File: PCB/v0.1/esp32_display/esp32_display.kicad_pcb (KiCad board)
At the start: 2 copper layers, 90.5 x 69 mm, 52 parts, among them J1 USB_B_Micro, J2 Conn_01x06_Male, SW1 RST_BTN, SW2 SCREEN_OFF_BTN, U1 ESP32-WROOM-32, U2 MAX1821, U3 Display_ILI9341

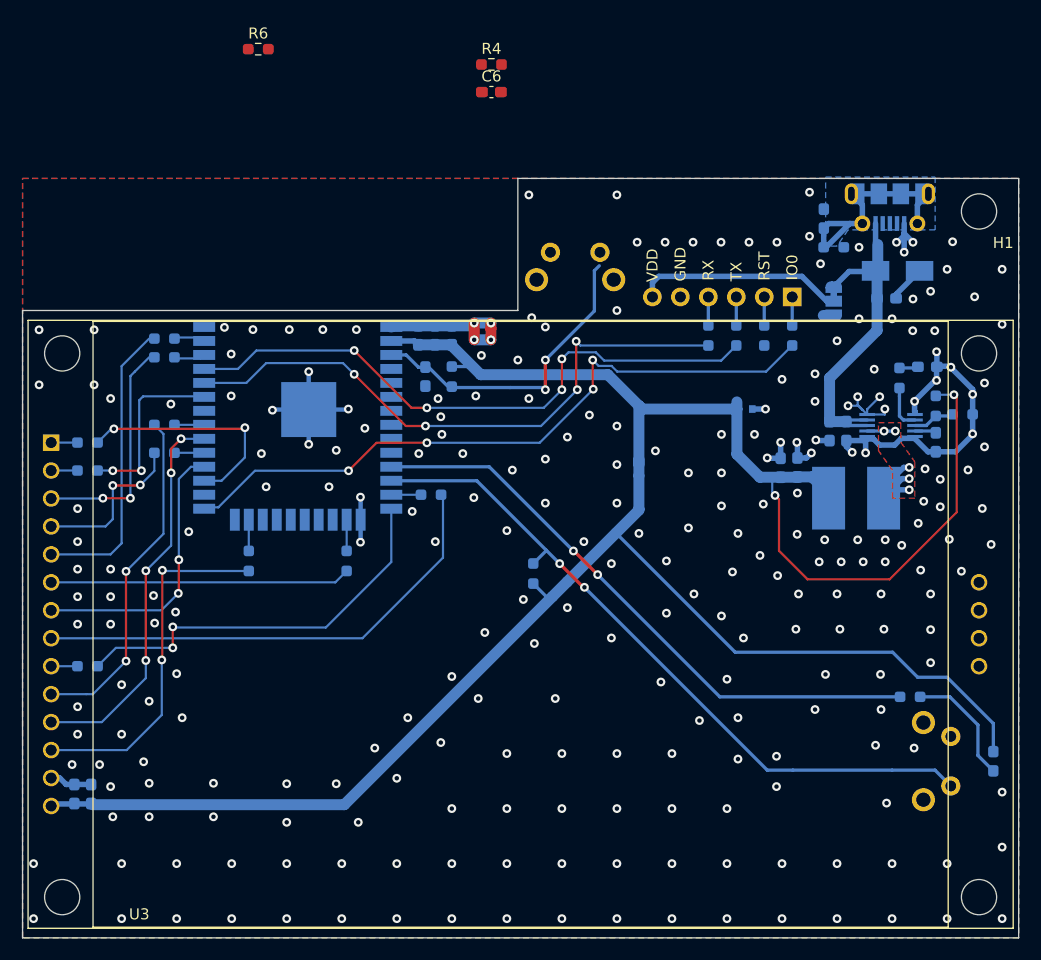
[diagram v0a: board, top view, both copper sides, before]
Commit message: Place RC filters (close to buttons)
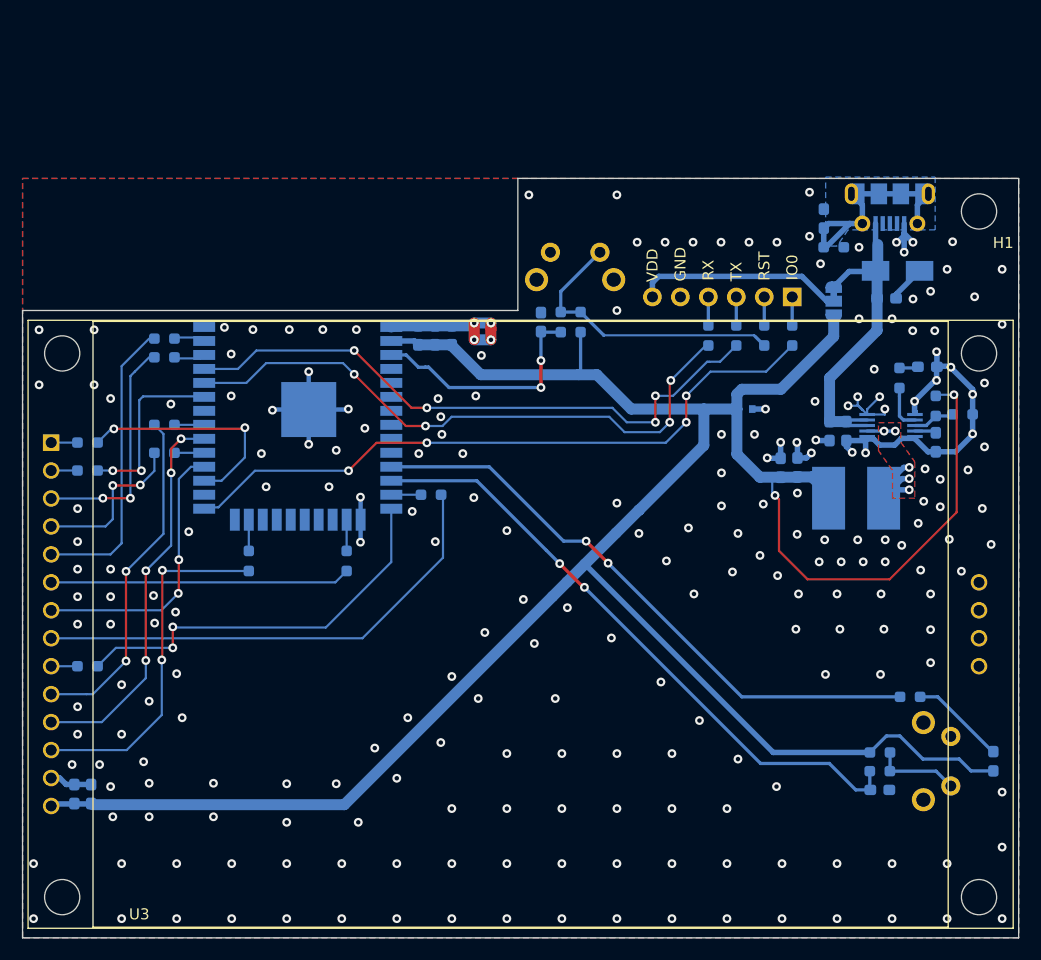
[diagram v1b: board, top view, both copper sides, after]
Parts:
- C6, R4, R6: moved to B.Cu
- moved R4 73.3 mm to (164.9, 85.9)
- moved C6 72.6 mm to (164.9, 87.6)
- moved R6 37.0 mm to (135.9, 45.1), turned to -90 degrees
- moved R3 35.4 mm to (164.9, 84.2), turned to 0 degrees
- moved R5 12.7 mm to (137.7, 45.1), turned to 90 degrees
- moved C7 11.6 mm to (134.1, 45.1), turned to 90 degrees
- turned D3 to -90 degrees
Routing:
- net /MCU/SCRN_OFF_BTN: track 0.00 -> 56.9 mm, vias 0 -> 2
- net Net-(R3-Pad2): track 64.0 -> 7.80 mm, vias 2 -> 0
- net /MCU/RST: track 0.00 -> 26.7 mm
- net +3V3: track 212.1 -> 228.3 mm
- net Net-(C7-Pad1): track 28.6 -> 21.7 mm
- net Net-(D3-Pad1): track 11.1 -> 8.71 mm
- net /MCU/IO0: track 62.1 -> 61.0 mm
- net GND: vias 258 -> 229

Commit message: Dont route L of buck converter through vias
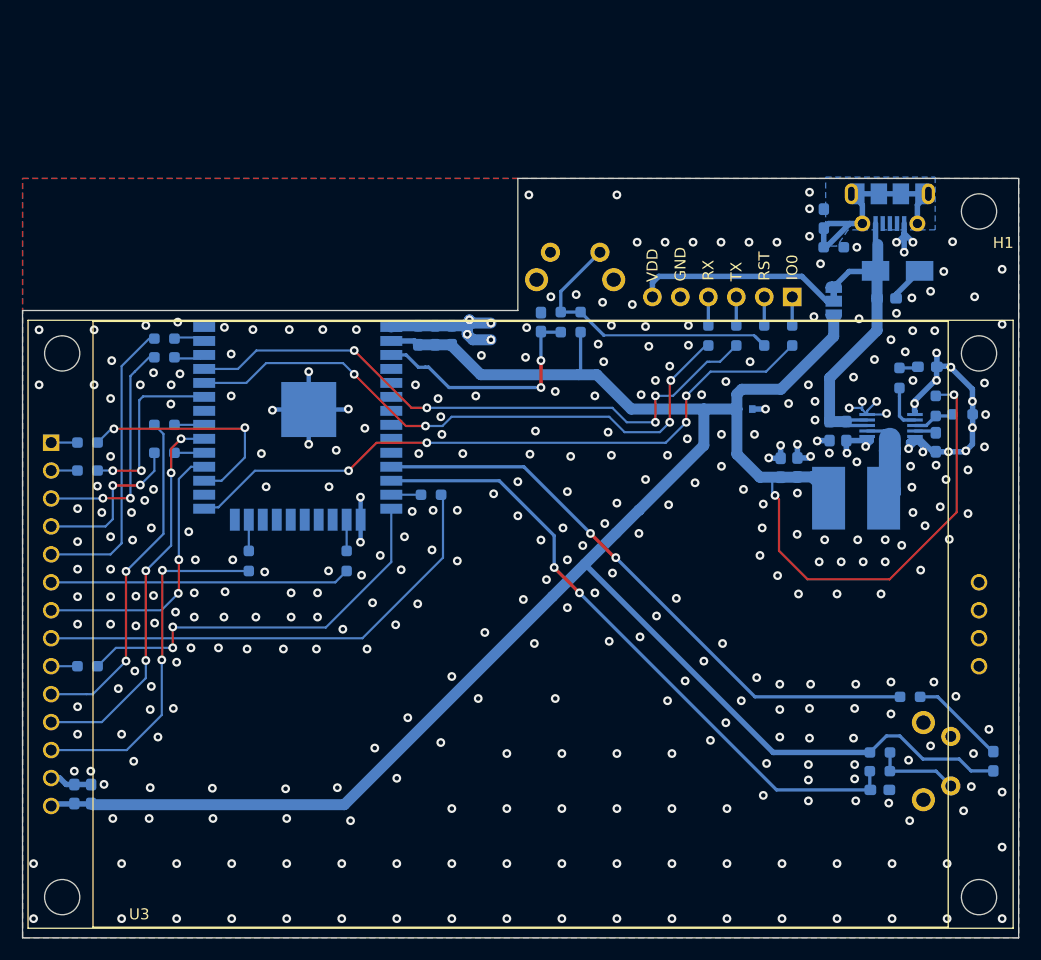
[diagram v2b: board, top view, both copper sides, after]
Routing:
- net GND: track 89.9 -> 84.6 mm, vias 229 -> 361
- net Net-(L1-Pad1): track 11.4 -> 8.19 mm, vias 5 -> 0
- net /MCU/SCRN_OFF_BTN: track 56.9 -> 58.6 mm
- removed copper zone on F.Cu, net Net-(L1-Pad1)

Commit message: Fix 3d models, generate outputs, add .wrl to outputs
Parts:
- J1: footprint Connector_USB:USB_Micro-B_Molex-105017-0001 -> myLib:USB_Micro-B_Molex-105017-0001

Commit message: Buck converter feedback line on top
PCB name and version generated with KiBuzzard
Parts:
- removed the G*** at (148.9, 90.8)
- added G***: LOGO, myLib:tabaluga_5x5, B.Cu at (103.2, 92.8)
- added kibuzzard-61D6E91A: G***, kibuzzard-61D6E91A, B.Cu at (137.2, 81.7)
- moved R19 2.81 mm to (172.6, 53.6), turned to 180 degrees
- moved R20 2.09 mm to (170.8, 52.1), turned to 180 degrees
- moved L1 0.47 mm to (162.7, 60.6)
- moved C10 0.33 mm to (170.0, 56.3)
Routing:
- net GND: track 84.6 -> 74.4 mm, vias 361 -> 367
- net +3V3: track 228.3 -> 224.8 mm, vias 2 -> 0
- net Net-(R19-Pad2): track 3.84 -> 5.48 mm
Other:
- board text added: "BCKL_OFF"
- board text removed: "DISP_OFF_BTN"
- board text removed: "ESP32_display v0.1"
